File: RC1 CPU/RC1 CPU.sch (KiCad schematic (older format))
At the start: 51 parts, among them J1 Expansion, J2 RC1_UI_Port, J3 BARREL_JACK, M1 Mounting, M2 Mounting, M3 Mounting, M4 Mounting, U1 WD65C02, U2 HM62256BLP-7, U3 28C256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

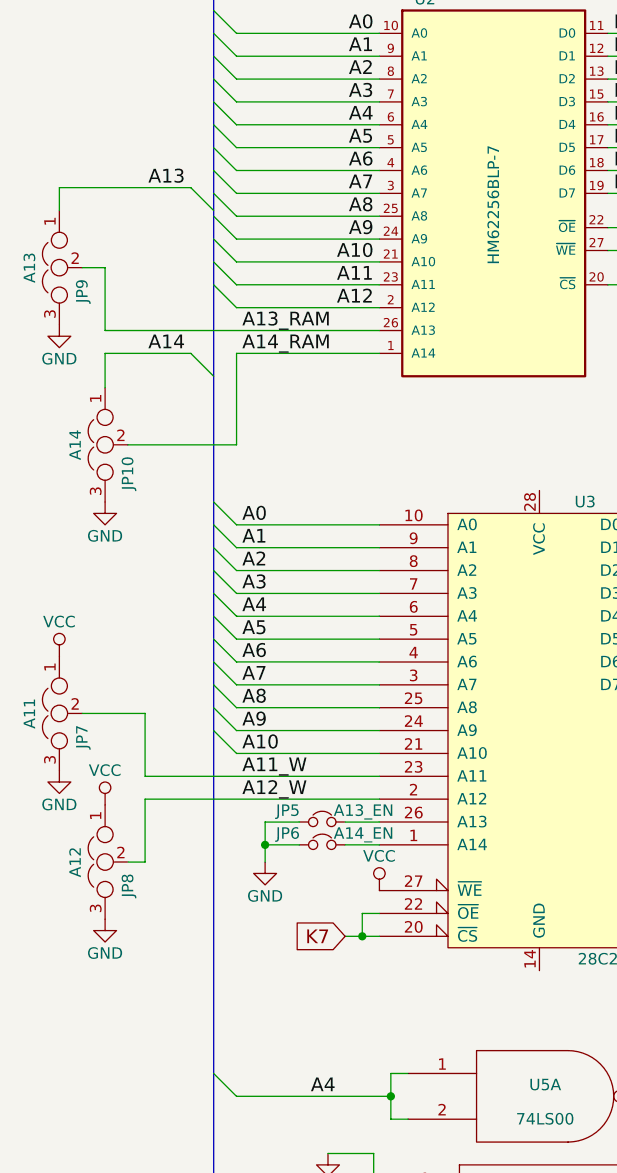
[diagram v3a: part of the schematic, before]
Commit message: Decided to connect remaining RAM address lines for external logic.
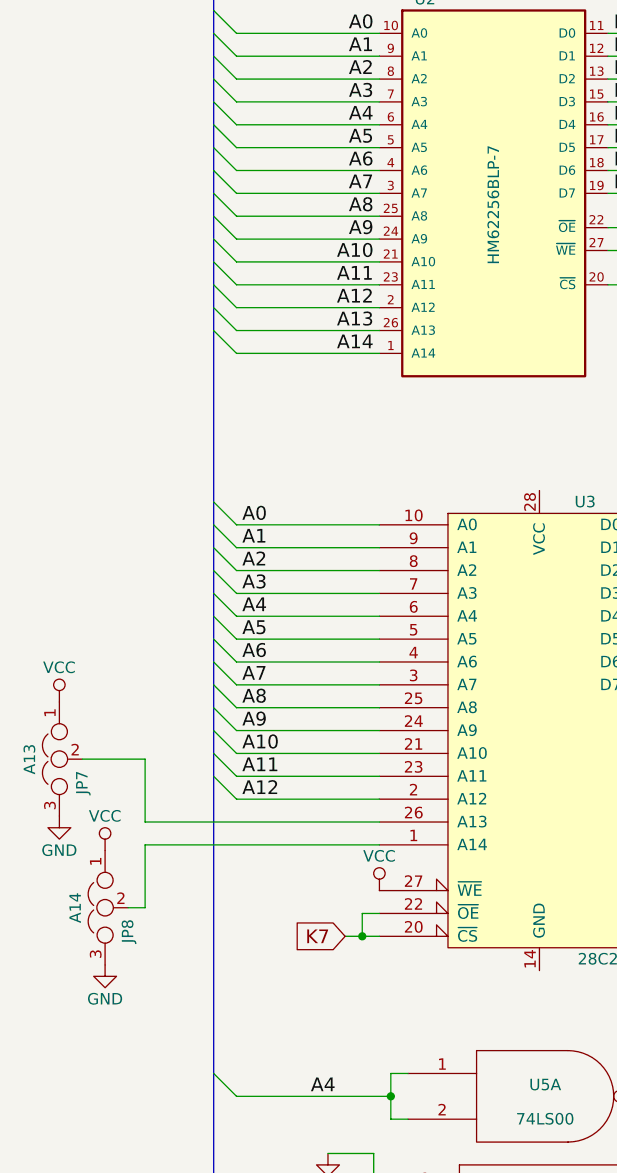
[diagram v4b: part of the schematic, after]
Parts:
- removed JP10: A14, Pin_Headers:Pin_Header_Straight_1x03_Pitch2.54mm, symbol Jumper_NC_Dual
- removed JP5: A13_EN, Pin_Headers:Pin_Header_Straight_1x02_Pitch2.54mm, symbol Jumper_NC_Small
- removed JP6: A14_EN, Pin_Headers:Pin_Header_Straight_1x02_Pitch2.54mm, symbol Jumper_NC_Small
- removed JP9: A13, Pin_Headers:Pin_Header_Straight_1x03_Pitch2.54mm, symbol Jumper_NC_Dual
- JP7: value A11 -> A13
- JP8: value A12 -> A14
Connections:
- net A13_RAM is gone; now on net A13: U2.26 (A13)
- net A14_RAM is gone; now on net A14: U2.1 (A14)
- net A11: now also U3.23 (A11)
- net A12: now also U3.2 (A12)
- net at U3.1 (A14): now also JP8.2
- net at U3.26 (A13): now also JP7.2
- removed net A11_W: JP7.2, U3.23 (A11)
- removed net A12_W: JP8.2, U3.2 (A12)
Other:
- moved on the sheet: JP7, JP8
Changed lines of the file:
@@
 Text Label 1475 7075 0    60   ~ 0
 A10
-$Comp
-L GND #PWR7
-U 1 1 5D67A3F5
-P 1575 7550
-F 0 "#PWR7" H 1575 7300 50  0001 C CNN
-F 1 "GND" H 1575 7400 50  0000 C CNN
-F 2 "" H 1575 7550 50  0001 C CNN
-F 3 "" H 1575 7550 50  0001 C CNN
-	1    1575 7550
-	1    0    0    -1
-$EndComp
 Text Label 3450 9675 0    60   ~ 0
 D0
@@
 K7 - ROM
 NoConn ~ 5475 9175
-$Comp
-L Jumper_NC_Small JP5
-U 1 1 5D768D80
-P 1825 7375
-F 0 "JP5" H 1675 7425 50  0000 C CNN
-F 1 "A13_EN" H 1875 7425 50  0000 L CNN
-F 2 "Pin_Headers:Pin_Header_Straight_1x02_Pitch2.54mm" H 1825 7375 50  0001 C CNN
-F 3 "" H 1825 7375 50  0001 C CNN
-	1    1825 7375
-	1    0    0    -1
-$EndComp
 Wire Wire Line
 	15750 1150 15850 1150
@@
 	1450 6875 2075 6875
 Wire Wire Line
-	1575 7375 1575 7550
-Connection ~ 1575 7475
-Wire Wire Line
 	3425 9675 3850 9675
 Wire Wire Line
@@
 	11375 10900 11575 10900
 Wire Wire Line
-	1050 7175 2075 7175
+	1050 7375 2075 7375
 Wire Wire Line
 	4850 3225 4075 3225
@@
 Wire Notes Line
 	6650 5950 6650 5475
-Wire Wire Line
-	1575 7375 1725 7375
-$Comp
-L Jumper_NC_Small JP6
-U 1 1 5D76A64A
-P 1825 7475
-F 0 "JP6" H 1675 7525 50  0000 C CNN
-F 1 "A14_EN" H 1875 7525 50  0000 L CNN
-F 2 "Pin_Headers:Pin_Header_Straight_1x02_Pitch2.54mm" H 1825 7475 50  0001 C CNN
-F 3 "" H 1825 7475 50  0001 C CNN
-	1    1825 7475
-	1    0    0    -1
-$EndComp
-Wire Wire Line
-	1575 7475 1725 7475
-Wire Wire Line
-	1925 7375 2075 7375
-Wire Wire Line
-	1925 7475 2075 7475
 Wire Bus Line
 	14300 950  1350 950
@@
 L Jumper_NC_Dual JP7
 U 1 1 5D779B66
-P 675 6900
-F 0 "JP7" H 725 6800 50  0000 L CNN
-F 1 "A11" H 675 7000 50  0000 C BNN
-F 2 "Pin_Headers:Pin_Header_Straight_1x03_Pitch2.54mm" H 675 6900 50  0001 C CNN
-F 3 "" H 675 6900 50  0001 C CNN
-	1    675  6900
+P 675 7100
+F 0 "JP7" H 725 7000 50  0000 L CNN
+F 1 "A13" H 675 7200 50  0000 C BNN
+F 2 "Pin_Headers:Pin_Header_Straight_1x03_Pitch2.54mm" H 675 7100 50  0001 C CNN
+F 3 "" H 675 7100 50  0001 C CNN
+	1    675  7100
 	0    -1   1    0
 $EndComp
@@
 L GND #PWR3
 U 1 1 5D77A162
-P 675 7150
-F 0 "#PWR3" H 675 6900 50  0001 C CNN
-F 1 "GND" H 675 7000 50  0000 C CNN
-F 2 "" H 675 7150 50  0001 C CNN
-F 3 "" H 675 7150 50  0001 C CNN
-	1    675  7150
+P 675 7350
+F 0 "#PWR3" H 675 7100 50  0001 C CNN
+F 1 "GND" H 675 7200 50  0000 C CNN
+F 2 "" H 675 7350 50  0001 C CNN
+F 3 "" H 675 7350 50  0001 C CNN
+	1    675  7350
 	1    0    0    -1
 $EndComp
@@
 L VCC #PWR2
 U 1 1 5D77A569
-P 675 6650
-F 0 "#PWR2" H 675 6500 50  0001 C CNN
-F 1 "VCC" H 675 6800 50  0000 C CNN
-F 2 "" H 675 6650 50  0001 C CNN
-F 3 "" H 675 6650 50  0001 C CNN
-	1    675  6650
+P 675 6850
+F 0 "#PWR2" H 675 6700 50  0001 C CNN
+F 1 "VCC" H 675 7000 50  0000 C CNN
+F 2 "" H 675 6850 50  0001 C CNN
+F 3 "" H 675 6850 50  0001 C CNN
+	1    675  6850
 	1    0    0    -1
 $EndComp
@@
 L Jumper_NC_Dual JP8
 U 1 1 5D77AA4F
-P 875 7550
-F 0 "JP8" H 925 7450 50  0000 L CNN
-F 1 "A12" H 875 7650 50  0000 C BNN
-F 2 "Pin_Headers:Pin_Header_Straight_1x03_Pitch2.54mm" H 875 7550 50  0001 C CNN
-F 3 "" H 875 7550 50  0001 C CNN
-	1    875  7550
+P 875 7750
+F 0 "JP8" H 925 7650 50  0000 L CNN
+F 1 "A14" H 875 7850 50  0000 C BNN
+F 2 "Pin_Headers:Pin_Header_Straight_1x03_Pitch2.54mm" H 875 7750 50  0001 C CNN
+F 3 "" H 875 7750 50  0001 C CNN
+	1    875  7750
 	0    -1   1    0
 $EndComp
@@
 L GND #PWR6
 U 1 1 5D77AA55
-P 875 7800
-F 0 "#PWR6" H 875 7550 50  0001 C CNN
-F 1 "GND" H 875 7650 50  0000 C CNN
-F 2 "" H 875 7800 50  0001 C CNN
-F 3 "" H 875 7800 50  0001 C CNN
-	1    875  7800
+P 875 8000
+F 0 "#PWR6" H 875 7750 50  0001 C CNN
+F 1 "GND" H 875 7850 50  0000 C CNN
+F 2 "" H 875 8000 50  0001 C CNN
+F 3 "" H 875 8000 50  0001 C CNN
+	1    875  8000
 	1    0    0    -1
 $EndComp
@@
 L VCC #PWR5
 U 1 1 5D77AA5B
-P 875 7300
-F 0 "#PWR5" H 875 7150 50  0001 C CNN
-F 1 "VCC" H 875 7450 50  0000 C CNN
-F 2 "" H 875 7300 50  0001 C CNN
-F 3 "" H 875 7300 50  0001 C CNN
-	1    875  7300
-	1    0    0    -1
-$EndComp
-Wire Wire Line
-	2075 7275 1050 7275
-Wire Wire Line
-	1050 7275 1050 7550
-Wire Wire Line
-	1050 7550 975  7550
-Wire Wire Line
-	1050 7175 1050 6900
-Wire Wire Line
-	1050 6900 775  6900
+P 875 7500
+F 0 "#PWR5" H 875 7350 50  0001 C CNN
+F 1 "VCC" H 875 7650 50  0000 C CNN
+F 2 "" H 875 7500 50  0001 C CNN
+F 3 "" H 875 7500 50  0001 C CNN
+	1    875  7500
+	1    0    0    -1
+$EndComp
+Wire Wire Line
+	2075 7475 1050 7475
+Wire Wire Line
+	1050 7475 1050 7750
+Wire Wire Line
+	1050 7750 975  7750
+Wire Wire Line
+	1050 7375 1050 7100
+Wire Wire Line
+	1050 7100 775  7100
+Entry Wire Line
+	1350 5125 1450 5225
+Entry Wire Line
+	1350 5225 1450 5325
+Text Label 2050 5225 2    60   ~ 0
+A13
+Text Label 2050 5325 2    60   ~ 0
+A14
+Wire Wire Line
+	1450 5225 2075 5225
+Wire Wire Line
+	1450 5325 2075 5325
+Entry Wire Line
+	1350 7075 1450 7175
 Text Label 1475 7175 0    60   ~ 0
-A11_W
+A11
+Wire Wire Line
+	1450 7175 2075 7175
+Entry Wire Line
+	1350 7175 1450 7275
 Text Label 1475 7275 0    60   ~ 0
-A12_W
-Wire Wire Line
-	875  5225 2075 5225
-$Comp
-L Jumper_NC_Dual JP9
-U 1 1 5D783AAF
-P 675 4950
-F 0 "JP9" H 725 4850 50  0000 L CNN
-F 1 "A13" H 675 5050 50  0000 C BNN
-F 2 "Pin_Headers:Pin_Header_Straight_1x03_Pitch2.54mm" H 675 4950 50  0001 C CNN
-F 3 "" H 675 4950 50  0001 C CNN
-	1    675  4950
-	0    -1   1    0
-$EndComp
-$Comp
-L GND #PWR1
-U 1 1 5D783AB5
-P 675 5200
-F 0 "#PWR1" H 675 4950 50  0001 C CNN
-F 1 "GND" H 675 5050 50  0000 C CNN
-F 2 "" H 675 5200 50  0001 C CNN
-F 3 "" H 675 5200 50  0001 C CNN
-	1    675  5200
-	1    0    0    -1
-$EndComp
-$Comp
-L Jumper_NC_Dual JP10
-U 1 1 5D783AC1
-P 875 5725
-F 0 "JP10" H 925 5625 50  0000 L CNN
-F 1 "A14" H 875 5825 50  0000 C BNN
-F 2 "Pin_Headers:Pin_Header_Straight_1x03_Pitch2.54mm" H 875 5725 50  0001 C CNN
-F 3 "" H 875 5725 50  0001 C CNN
-	1    875  5725
-	0    -1   1    0
-$EndComp
-$Comp
-L GND #PWR4
-U 1 1 5D783AC7
-P 875 5975
-F 0 "#PWR4" H 875 5725 50  0001 C CNN
-F 1 "GND" H 875 5825 50  0000 C CNN
-F 2 "" H 875 5975 50  0001 C CNN
-F 3 "" H 875 5975 50  0001 C CNN
-	1    875  5975
-	1    0    0    -1
-$EndComp
-Wire Wire Line
-	975  5725 1450 5725
-Entry Wire Line
-	1250 5325 1350 5425
-Wire Wire Line
-	1250 5325 875  5325
-Wire Wire Line
-	875  5325 875  5475
-Wire Wire Line
-	1450 5725 1450 5325
-Wire Wire Line
-	1450 5325 2075 5325
-Wire Wire Line
-	675  4700 675  4600
-Wire Wire Line
-	675  4600 1250 4600
-Entry Wire Line
-	1250 4600 1350 4700
-Text Label 1225 4600 2    60   ~ 0
-A13
-Text Label 1225 5325 2    60   ~ 0
-A14
-Wire Wire Line
-	875  5225 875  4950
-Wire Wire Line
-	875  4950 775  4950
-Text Label 1475 5225 0    60   ~ 0
-A13_RAM
-Text Label 1475 5325 0    60   ~ 0
-A14_RAM
+A12
+Wire Wire Line
+	1450 7275 2075 7275
 $EndSCHEMATC

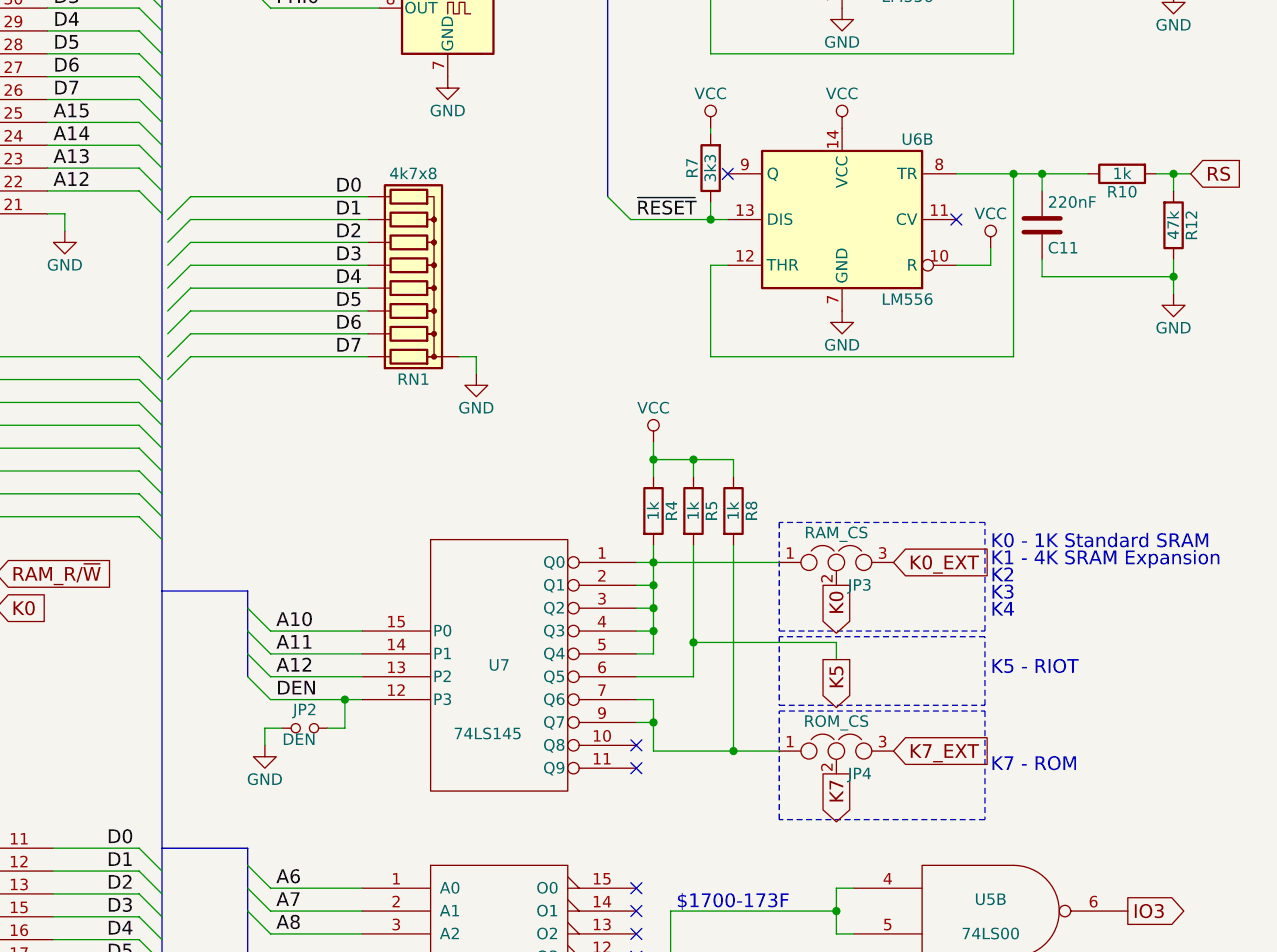
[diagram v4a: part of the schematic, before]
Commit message: 65K Expansion schematic done
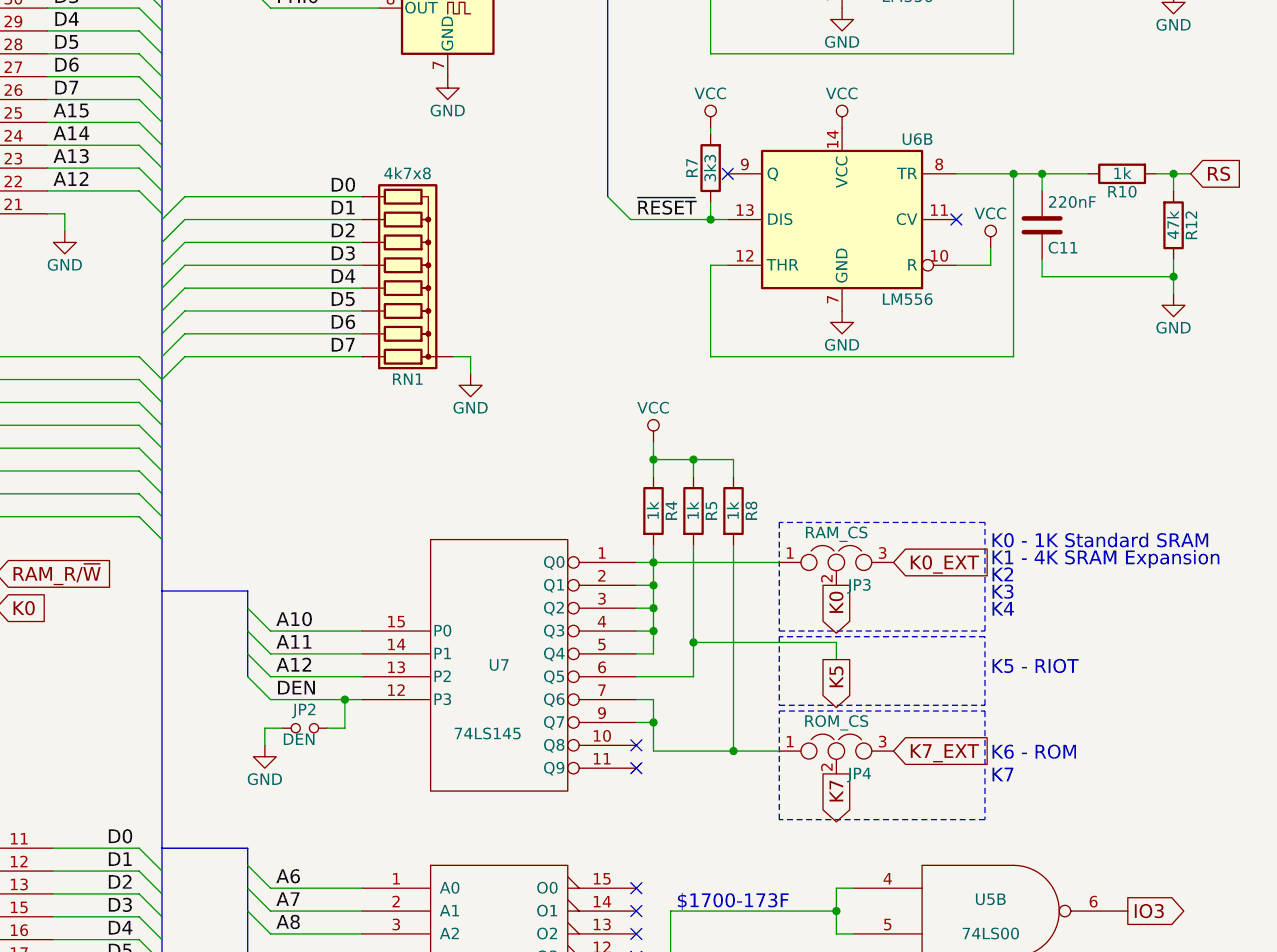
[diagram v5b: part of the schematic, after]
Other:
- note added: "K6 - ROM"
- note added: "K7"
- note removed: "K7 - ROM"
- moved on the sheet: RN1
